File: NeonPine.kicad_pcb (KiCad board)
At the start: 2 copper layers, 54.7 x 69 mm, 98 parts, among them J1 USB-C 6P (USB4125-GF-A), J2 SWD pogo pads, Q1 DMN15H310SE, Q11 MMDT5551, Q12 MMDT5551, Q13 MMDT5551, Q14 MMDT5551, Q15 MMDT5551, Q16 MMDT5551, Q17 MMDT5551, Q18 MMDT5551, Q19 MMDT5551, Q2 TEPT4400, Q20 MMDT5551, U1 CH32V003F4P6, U2 74HC595BQ, U3 74HC595BQ

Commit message: Cleanup, prod test
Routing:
- net /LAMP1: track 34.3 -> 33.6 mm
- net Net-(Q13B-C2): vias 1 -> 0
- net /SR_CHAIN: vias 3 -> 2
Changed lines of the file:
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@@
 		(net "Net-(Q13A-C1)")
 	)
-	(via
-		(at 105.338 68.35)
-		(size 0.7)
-		(drill 0.35)
-		(layers "F.Cu" "B.Cu")
-		(net "Net-(Q13B-C2)")
-	)
 	(segment
 		(start 106.107624 61.5)
@@
 	)
 	(segment
-		(start 102.2 53.71)
-		(end 102.2 54.4523)
-		(width 0.15)
-		(layer "B.Cu")
-		(net "/LAMP1")
-	)
-	(segment
 		(start 97.5 81.0625)
 		(end 97.5 80.349516)
@@
 		(size 0.6)
 		(drill 0.3)
-		(layers "F.Cu" "B.Cu")
-		(net "/SR_CHAIN")
-	)
-	(via
-		(at 115.268 100.196)
-		(size 0.6)
-		(drill 0.3)

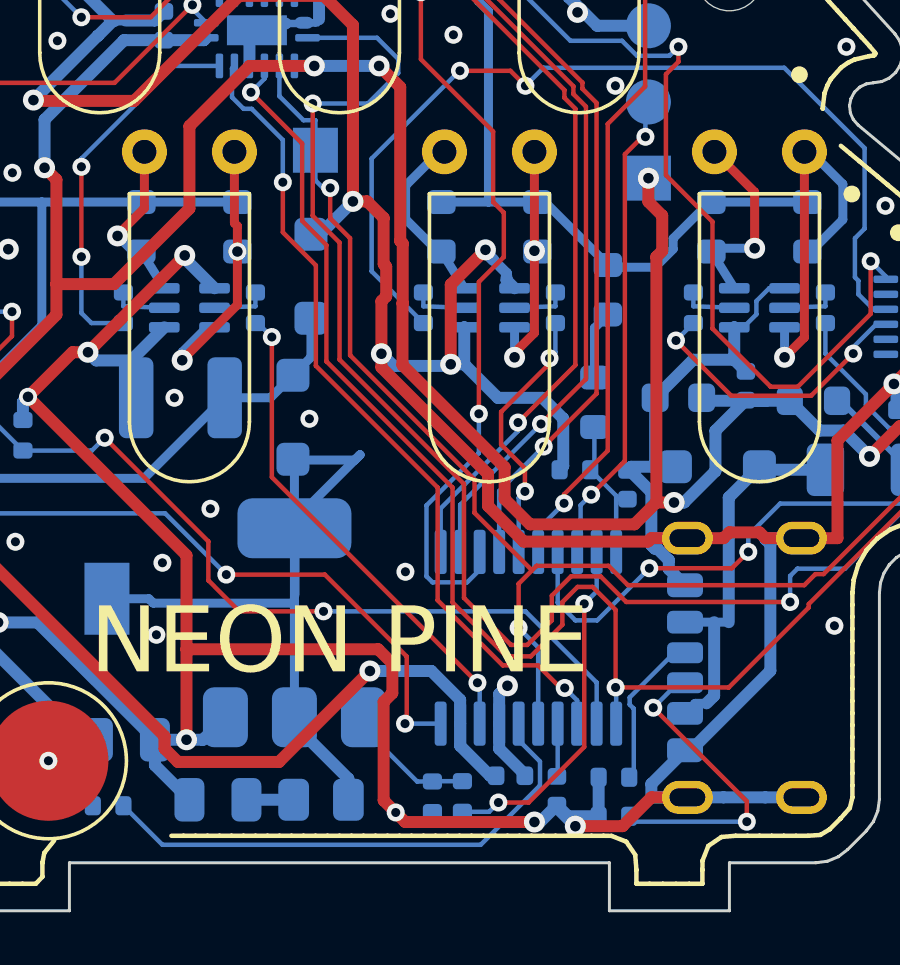
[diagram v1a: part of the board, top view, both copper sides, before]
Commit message: prep
moved MCU to left
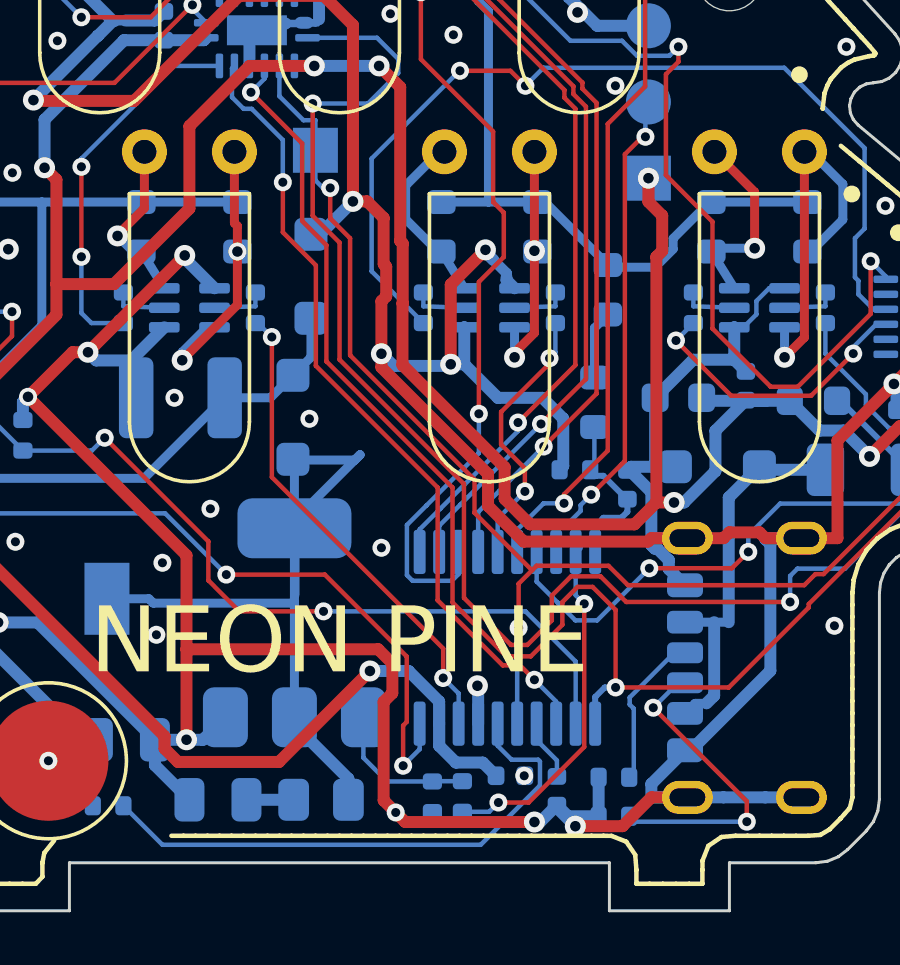
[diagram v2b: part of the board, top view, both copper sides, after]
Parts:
- moved U1 0.70 mm to (105.6, 102.5)
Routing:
- net GND: track 290.4 -> 288.2 mm, vias 68 -> 69
- net /LAMP7: track 29.2 -> 31.1 mm
- net /TOUCH2: track 17.6 -> 18.4 mm
- net /VFB: track 4.95 -> 5.68 mm
- net /SR_DATA: track 27.7 -> 26.9 mm
- net /LAMP6: track 21.4 -> 22.1 mm
- net /GATE: track 4.40 -> 4.98 mm
- net /LAMP9: track 8.79 -> 9.38 mm
- net /SR_LATCH: track 53.2 -> 53.7 mm

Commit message: done
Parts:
- removed C7: 100n, Capacitor_SMD:C_0402_1005Metric
- added D4: BZX884-C3V6, Diode_SMD:D_SOD-882, B.Cu at (107.1, 109.2)
- added D5: BZX884-C3V6, Diode_SMD:D_SOD-882, B.Cu at (108.8, 109.2)
- added R13: 68, Resistor_SMD:R_0402_1005Metric, B.Cu at (107.5, 107.7)
- added R14: 68, Resistor_SMD:R_0402_1005Metric, B.Cu at (108.9, 107.7)
- added R15: 1k5, Resistor_SMD:R_0402_1005Metric, B.Cu at (112.5, 109.4)
- J1: value USB-C 6P (USB4125-GF-A) -> USB-C 16P (USB4105-GF-A); footprint Connector_USB:USB_C_Receptacle_GCT_USB4125-xx-x_6P_TopMnt_Horizontal -> Connector_USB:USB_C_Receptacle_GCT_USB4105-xx-A_16P_TopMnt_Horizontal
- moved R3 5.75 mm to (114.5, 109.4), turned to 0 degrees
- moved R4 1.72 mm to (110.6, 109.4), turned to 0 degrees
- moved J1 0.27 mm to (114.3, 103.5)
- moved C5 0.16 mm to (109.6, 97.2)
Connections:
- U1 pad 1: /SR_LATCH -> /USB_DM_MCU
- U1 pad 17: /LAMP10 -> /SR_CLK
- U1 pad 19: /GATE_DRV -> /USB_DP_MCU
- U1 pad 2: /LDR -> /SR_LATCH
- U1 pad 3: /SR_DATA -> /GATE_DRV
- U1 pad 4: /NRST -> /SR_DATA
- U1 pad 5: /SR_CLK -> /LDR
- U3 pad 3: unconnected-(U3-QD-Pad3) -> /LAMPA10
- U3 pad 4: /LAMPA10 -> /LAMP10
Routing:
- net GND: track 288.2 -> 243.5 mm, vias 69 -> 75
- net /LAMP10: track 24.8 -> 2.01 mm, vias 2 -> 0
- net /USB_DP: track 0.00 -> 12.8 mm, vias 0 -> 2
- net /USB_DM: track 0.00 -> 12.0 mm
- net /USB_DP_MCU: track 0.00 -> 8.33 mm, vias 0 -> 2
- net /VBUS: track 13.0 -> 20.0 mm
- net /GATE_DRV: track 11.7 -> 5.29 mm
- net /CC2: track 10.5 -> 4.89 mm, vias 2 -> 0
- net /SW: track 26.6 -> 21.2 mm
- net /SR_LATCH: track 53.7 -> 48.8 mm
- net /CC1: track 5.24 -> 9.44 mm, vias 0 -> 2
- net /SR_CHAIN: track 52.4 -> 48.4 mm
- net /SR_CLK: track 49.2 -> 45.5 mm
- net /LDR: track 34.2 -> 32.1 mm
- net /NRST: track 2.07 -> 0.00 mm
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
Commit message: USB clearance fix
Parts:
- moved J1 1.20 mm to (115.5, 103.5)
- moved F1 1.10 mm to (116.5, 96.8)
- moved D3 0.60 mm to (112.0, 96.8)
- moved C5 0.30 mm to (109.3, 97.2)
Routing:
- net /SR_LATCH: track 48.8 -> 50.1 mm
- net /SR_CHAIN: track 48.4 -> 49.7 mm
- net /CC1: track 9.44 -> 10.6 mm
- net /USB_DM: track 12.0 -> 13.1 mm
- net /USB_DP: track 12.8 -> 13.7 mm
- net /CC2: track 4.89 -> 5.72 mm
- net /VFB: track 5.74 -> 5.00 mm
- net /SR_CLK: track 45.5 -> 46.1 mm
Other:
- outline, holes or cut-outs redrawn
